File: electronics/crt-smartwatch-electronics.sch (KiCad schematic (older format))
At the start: 1 part

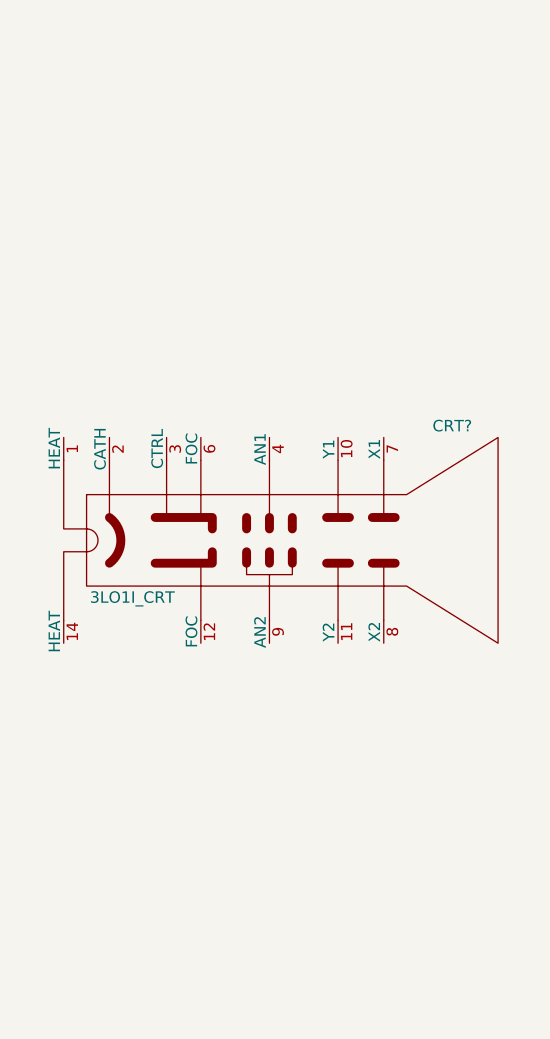
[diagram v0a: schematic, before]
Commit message: Initial connections to CRT
References:
http://www.cathodecorner.com/sc200/SC200CBoardManual.pdf
http://tubetime.us/index.php/2014/05/31/electrostatic-crt-driver-design/
https://www.youtube.com/watch?v=rDfs7nth5pQ
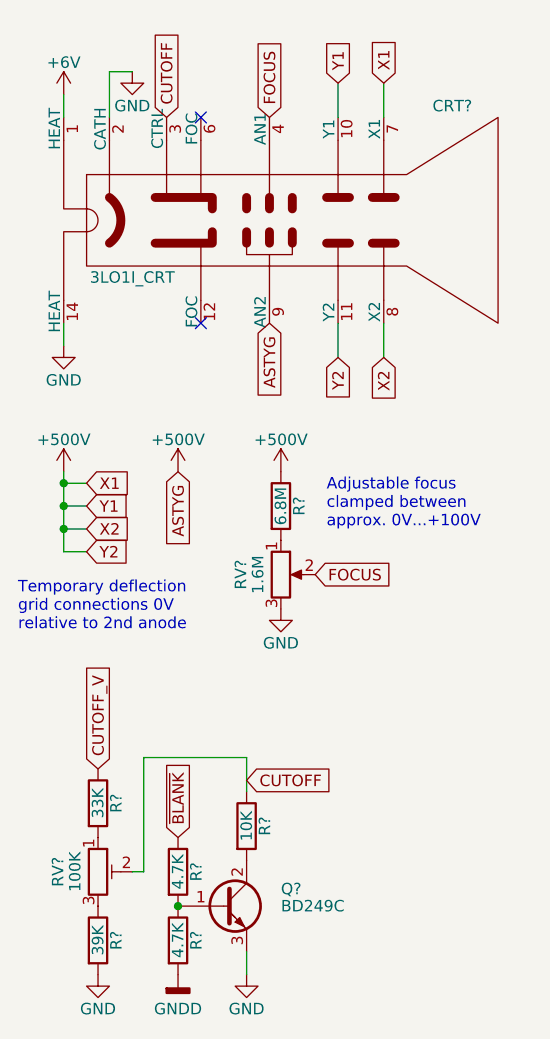
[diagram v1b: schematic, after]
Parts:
- added Q?: BD249C, symbol Transistor_BJT:BD249C
- added R?: 6.8M, symbol Device:R
- added R?: 33K, symbol Device:R
- added R?: 39K, symbol Device:R
- added R?: 10K, symbol Device:R
- added R? (x2): 4.7K, symbol Device:R
- added RV?: 1.6M, symbol Device:R_POT
- added RV?: 100K, symbol Device:R_POT_TRIM
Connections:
- net +6V: now reaches CRT?.1 (HEAT)
- net +500V: now reaches CRT?.10 (Y1)
- net +500V: now also CRT?.11 (Y2), CRT?.7 (X1), CRT?.8 (X2), CRT?.9 (AN2), R?.1
- net GND: now reaches CRT?.14 (HEAT)
- net GND: now also CRT?.2 (CATH), Q?.3 (E), R?.2, RV?.3
- net CUTOFF: now reaches CRT?.3 (CTRL)
- net CUTOFF: now also R?.1, RV?.2
- net FOCUS: now reaches CRT?.4 (AN1)
- net FOCUS: now also RV?.2
- new net: R?.2, RV?.1 (x2)
- new net: R?.1, RV?.3
- new net: Q?.1 (B), R?.1, R?.2
- new net: Q?.2 (C), R?.2
- new net CUTOFF_V: R?.1
- new net GNDD: R?.2
- new net ~BLANK: R?.1
- no-connect marks 0 -> 2
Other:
- note added: "Adjustable focus\nclamped between\napprox. 0V...+100V"
- note added: "Temporary deflection\ngrid connections 0V\nrelative to 2nd anode"
- moved on the sheet: CRT?

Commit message: Footprint for tube socket (PL-31) ordered from Amazon
https://www.amazon.com/Sockets-3LO1I-5LO2I-6LO1I-6LO2I/dp/B07Q468DZ4
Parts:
- CRT?: footprint (none) -> crt-smartwatch-footprints:PL-31_Socket
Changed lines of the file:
@@
 F 0 "CRT?" H 10800 2050 50  0000 C CNN
 F 1 "3LO1I_CRT" H 9400 1300 50  0000 C CNN
-F 2 "" H 9400 1550 50  0001 C CNN
+F 2 "crt-smartwatch-footprints:PL-31_Socket" H 9400 1550 50  0001 C CNN
 F 3 "" H 9400 1550 50  0001 C CNN
 	1    10000 1550
@@
 FOCUS
 $Comp
-L power:GND #PWR?
+L power:GND #PWR0101
 U 1 1 60A33D9B
 P 9100 2100
-F 0 "#PWR?" H 9100 1850 50  0001 C CNN
+F 0 "#PWR0101" H 9100 1850 50  0001 C CNN
 F 1 "GND" H 9100 1950 50  0000 C CNN
 F 2 "" H 9100 2100 50  0001 C CNN
@@
 	9100 2000 9100 2100
 $Comp
-L power:+6V #PWR?
+L power:+6V #PWR0102
 U 1 1 60A34C57
 P 9100 1000
-F 0 "#PWR?" H 9100 850 50  0001 C CNN
+F 0 "#PWR0102" H 9100 850 50  0001 C CNN
 F 1 "+6V" H 9100 1140 50  0000 C CNN
 F 2 "" H 9100 1000 50  0001 C CNN
@@
 	9300 900  9300 1100
 $Comp
-L power:GND #PWR?
+L power:GND #PWR0103
 U 1 1 60A36F3D
 P 9400 900
-F 0 "#PWR?" H 9400 650 50  0001 C CNN
+F 0 "#PWR0103" H 9400 650 50  0001 C CNN
 F 1 "GND" H 9400 750 50  0000 C CNN
 F 2 "" H 9400 900 50  0001 C CNN
@@
 FOCUS
 $Comp
-L crt-smartwatch-symbols:+500V #PWR?
+L crt-smartwatch-symbols:+500V #PWR0104
 U 1 1 60A40430
 P 10050 2650
-F 0 "#PWR?" H 10050 2500 50  0001 C CNN
+F 0 "#PWR0104" H 10050 2500 50  0001 C CNN
 F 1 "+500V" H 10050 2790 50  0000 C CNN
 F 2 "" H 10050 2650 50  0001 C CNN
@@
 $EndComp
 $Comp
-L power:GND #PWR?
+L power:GND #PWR0105
 U 1 1 60A40F16
 P 10050 3250
-F 0 "#PWR?" H 10050 3000 50  0001 C CNN
+F 0 "#PWR0105" H 10050 3000 50  0001 C CNN
 F 1 "GND" H 10050 3100 50  0000 C CNN
 F 2 "" H 10050 3250 50  0001 C CNN
@@
 Connection ~ 9100 2700
 $Comp
-L crt-smartwatch-symbols:+500V #PWR?
+L crt-smartwatch-symbols:+500V #PWR0106
 U 1 1 60A57ED2
 P 9100 2650
-F 0 "#PWR?" H 9100 2500 50  0001 C CNN
+F 0 "#PWR0106" H 9100 2500 50  0001 C CNN
 F 1 "+500V" H 9100 2790 50  0000 C CNN
 F 2 "" H 9100 2650 50  0001 C CNN
@@
 $EndComp
 $Comp
-L power:GND #PWR?
+L power:GND #PWR0107
 U 1 1 60A5EEAC
 P 9250 4850
-F 0 "#PWR?" H 9250 4600 50  0001 C CNN
+F 0 "#PWR0107" H 9250 4600 50  0001 C CNN
 F 1 "GND" H 9250 4700 50  0000 C CNN
 F 2 "" H 9250 4850 50  0001 C CNN
@@
 $EndComp
 $Comp
-L power:GND #PWR?
+L power:GND #PWR0108
 U 1 1 60A5F4D1
 P 9900 4850
-F 0 "#PWR?" H 9900 4600 50  0001 C CNN
+F 0 "#PWR0108" H 9900 4600 50  0001 C CNN
 F 1 "GND" H 9900 4700 50  0000 C CNN
 F 2 "" H 9900 4850 50  0001 C CNN
@@
 Connection ~ 9600 4550
 $Comp
-L power:GNDD #PWR?
+L power:GNDD #PWR0109
 U 1 1 60A6441E
 P 9600 4850
-F 0 "#PWR?" H 9600 4600 50  0001 C CNN
+F 0 "#PWR0109" H 9600 4600 50  0001 C CNN
 F 1 "GNDD" H 9600 4700 50  0000 C CNN
 F 2 "" H 9600 4850 50  0001 C CNN
@@
 ASTYG
 $Comp
-L crt-smartwatch-symbols:+500V #PWR?
+L crt-smartwatch-symbols:+500V #PWR0110
 U 1 1 60A77348
 P 9600 2650
-F 0 "#PWR?" H 9600 2500 50  0001 C CNN
+F 0 "#PWR0110" H 9600 2500 50  0001 C CNN
 F 1 "+500V" H 9600 2790 50  0000 C CNN
 F 2 "" H 9600 2650 50  0001 C CNN

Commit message: Battery monitoring circuit schematic
Reference BQ769x0 datasheet https://www.ti.com/product/BQ76920
TI also has a video helping with the schematic
https://www.youtube.com/watch?v=B5dsIc2C_xA
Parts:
- added BT?: LiPo_3s, symbol crt-smartwatch-symbols:LiPo_3s
- added C? (x2): 1u, symbol Device:C_Small
- added C? (x4): C_c, symbol Device:C_Small
- added C?: C_f, symbol Device:C_Small
- added C?: 4.7u, symbol Device:C_Small
- added C? (x3): 0.1u, symbol Device:C_Small
- added C?: 470p, symbol Device:C_Small
- added D?: 1N914, symbol Diode:1N914
- added J?: Balance, symbol Connector_Generic:Conn_01x04
- added J?: LiPo, symbol Connector_Generic:Conn_01x02
- added Q? (x2): 2N7000, Package_TO_SOT_THT:TO-92_Inline, symbol Transistor_FET:2N7000
- added Q?: VP0610L, Package_TO_SOT_THT:TO-92L_Inline, symbol Transistor_FET:VP0610L
- added R? (x4): R_c, symbol Device:R
- added R?: R_f, symbol Device:R
- added R?: R_sns, symbol Device:R
- added R? (x2): 100, symbol Device:R
- added R? (x3): 1M, symbol Device:R
- added R? (x2): 10k, symbol Device:R
- added R?: 510k, symbol Device:R
- added SW?: SW_Push, symbol Switch:SW_Push
- added U?: BQ7692006, Package_SO:TSSOP-20_4.4x6.5mm_P0.65mm, symbol Battery_Management:BQ76920PW
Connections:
- net GND: now also BT?.~ (Pack_-), C?.1, C?.1, C?.1, C?.2, C?.2, C?.2, C?.2, C?.2, C?.2, J?.2 (Pin_2), Q?.2 (G), R?.1, R?.1, R?.1, R?.1, U?.3 (VSS); no longer CRT?.14 (HEAT), CRT?.2 (CATH), Q?.3 (E), R?.2, RV?.3
- new net: C?.1, R?.2, U?.10 (BAT)
- new net: R?.1, R?.2, U?.6 (TS1)
- new net: C?.1, U?.7 (CAP1)
- new net: Q?.1 (S), R?.1, R?.1, R?.2
- new net: Q?.3 (D), Q?.3 (D)
- new net: D?.1 (K), Q?.2 (G), R?.1, R?.2
- new net: D?.2 (A), Q?.3 (D), R?.2
- new net: R?.2, SW?.1
- new net +3V3: C?.1, U?.8 (REGOUT)
- new net +BATT: BT?.~ (Pack_-), C?.2, J?.1 (Pin_1), R?.1, U?.9 (REGSRC)
- new net ALERT: C?.1, R?.2, U?.20 (ALERT)
- new net C0: C?.2, R?.2, U?.17 (VC0)
- new net C1: C?.1, C?.2, R?.2, SW?.2, U?.16 (VC1)
- new net C2: C?.1, C?.2, R?.2, U?.13 (VC4), U?.14 (VC3), U?.15 (VC2)
- new net C3: C?.1, R?.2, U?.12 (VC5)
- new net CELL_0: BT?.~ (Pack_-), J?.4 (Pin_4), R?.1
- new net CELL_1: BT?.~ (Pack_-), J?.3 (Pin_3), R?.1
- new net CELL_2: BT?.~ (Pack_-), J?.2 (Pin_2), R?.1
- new net CELL_3: BT?.~ (Pack_-), J?.1 (Pin_1), R?.1
- new net CHG: Q?.1 (S), U?.2 (CHG)
- new net DSG: Q?.2 (G), R?.2, U?.1 (DSG)
- new net GND1: CRT?.14 (HEAT), CRT?.2 (CATH), Q?.1 (S), Q?.3 (E), R?.1, R?.2, RV?.3
- new net SCL: U?.5 (SCL)
- new net SDA: U?.4 (SDA)
- new net SRN: C?.1, C?.2, R?.2, U?.19 (SRN)
- new net SRP: C?.1, C?.2, R?.2, U?.18 (SRP)
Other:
- note added: "Battery and connectors"
- note added: "Battery current measuring\nresistor and RC filters"
- note added: "Battery monitor IC"
- note added: "Cell voltage sensing RC filters"
- note added: "Low-side MOSFET power\ncuttoff circuit"

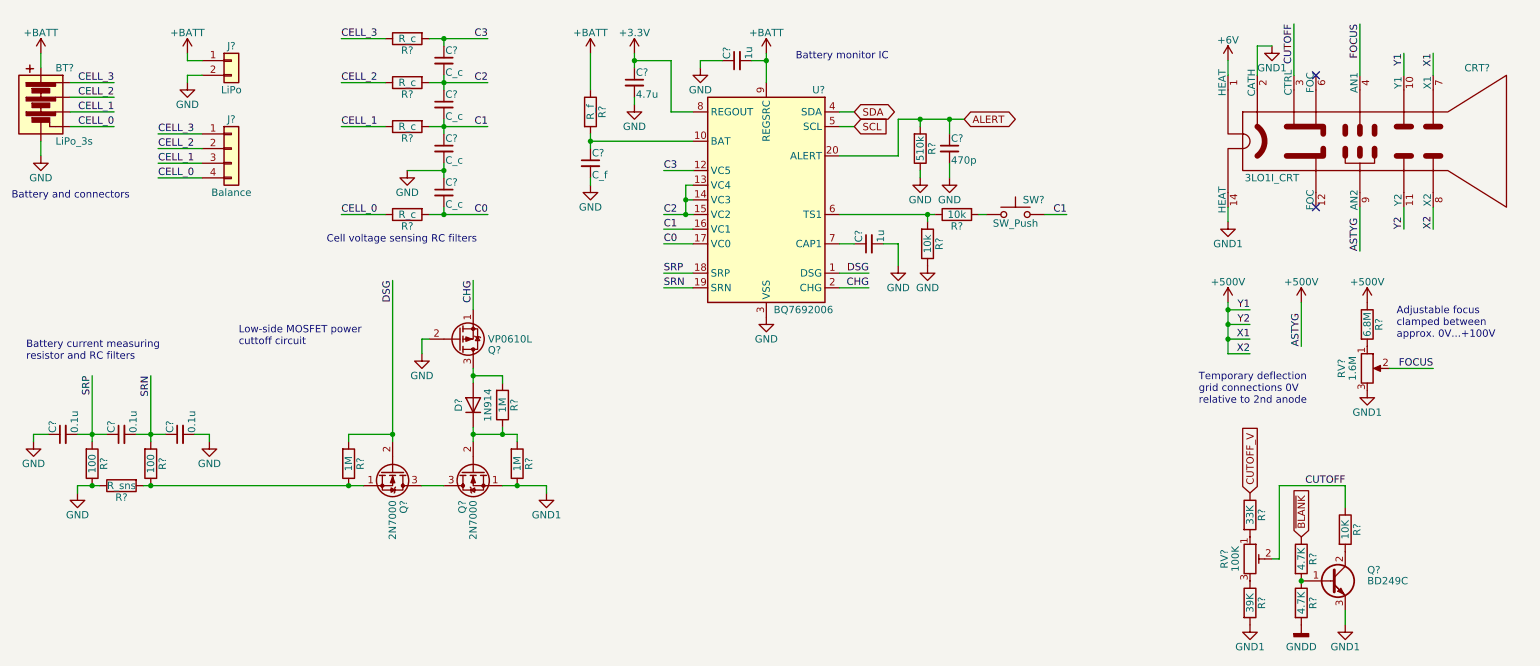
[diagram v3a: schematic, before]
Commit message: Compartmentalized schematic circuits into separate sheets
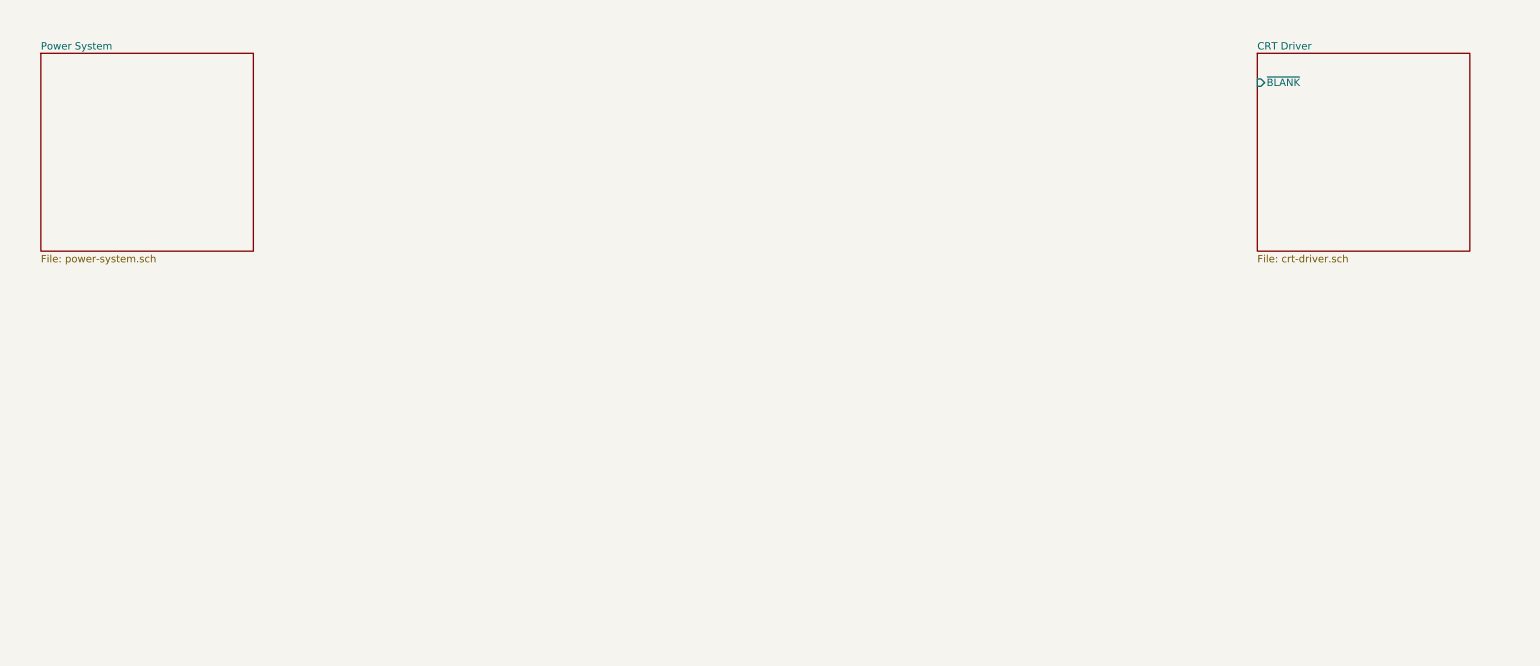
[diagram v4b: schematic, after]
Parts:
- removed BT?: LiPo_3s, symbol crt-smartwatch-symbols:LiPo_3s
- removed C? (x2): 1u, symbol Device:C_Small
- removed C? (x4): C_c, symbol Device:C_Small
- removed C?: C_f, symbol Device:C_Small
- removed C?: 4.7u, symbol Device:C_Small
- removed C? (x3): 0.1u, symbol Device:C_Small
- removed C?: 470p, symbol Device:C_Small
- removed CRT?: 3LO1I_CRT, crt-smartwatch-footprints:PL-31_Socket, symbol crt-smartwatch-symbols:3LO1I_CRT
- removed D?: 1N914, symbol Diode:1N914
- removed J?: Balance, symbol Connector_Generic:Conn_01x04
- removed J?: LiPo, symbol Connector_Generic:Conn_01x02
- removed Q?: BD249C, symbol Transistor_BJT:BD249C
- removed Q? (x2): 2N7000, Package_TO_SOT_THT:TO-92_Inline, symbol Transistor_FET:2N7000
- removed Q?: VP0610L, Package_TO_SOT_THT:TO-92L_Inline, symbol Transistor_FET:VP0610L
- removed R?: 6.8M, symbol Device:R
- removed R?: 33K, symbol Device:R
- removed R?: 39K, symbol Device:R
- removed R?: 10K, symbol Device:R
- removed R? (x2): 4.7K, symbol Device:R
- removed R? (x4): R_c, symbol Device:R
- removed R?: R_f, symbol Device:R
- removed R?: R_sns, symbol Device:R
- removed R? (x2): 100, symbol Device:R
- removed R? (x3): 1M, symbol Device:R
- removed R? (x2): 10k, symbol Device:R
- removed R?: 510k, symbol Device:R
- removed RV?: 1.6M, symbol Device:R_POT
- removed RV?: 100K, symbol Device:R_POT_TRIM
- removed SW?: SW_Push, symbol Switch:SW_Push
- removed U?: BQ7692006, Package_SO:TSSOP-20_4.4x6.5mm_P0.65mm, symbol Battery_Management:BQ76920PW
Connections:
- no-connect marks 2 -> 0
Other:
- note removed: "Adjustable focus\nclamped between\napprox. 0V...+100V"
- note removed: "Battery and connectors"
- note removed: "Battery current measuring\nresistor and RC filters"
- note removed: "Battery monitor IC"
- note removed: "Cell voltage sensing RC filters"
- note removed: "Low-side MOSFET power\ncuttoff circuit"
- note removed: "Temporary deflection\ngrid connections 0V\nrelative to 2nd anode"

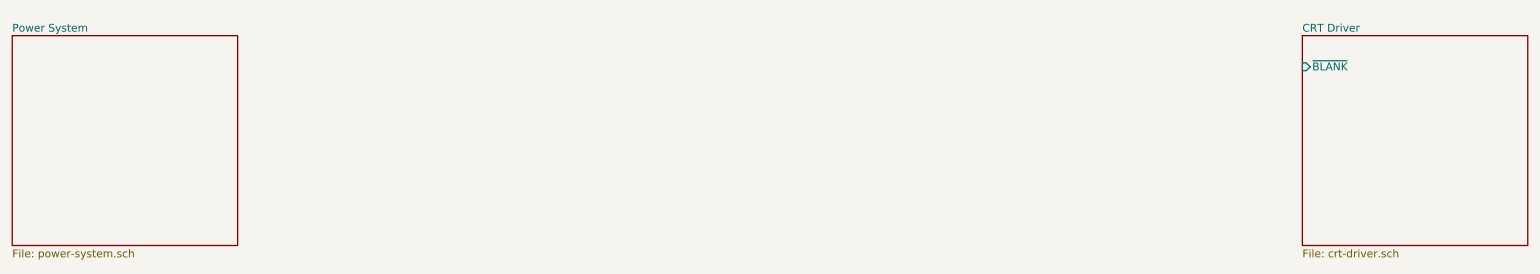
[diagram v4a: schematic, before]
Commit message: Design notes for 3.3V LDR and schematic updates
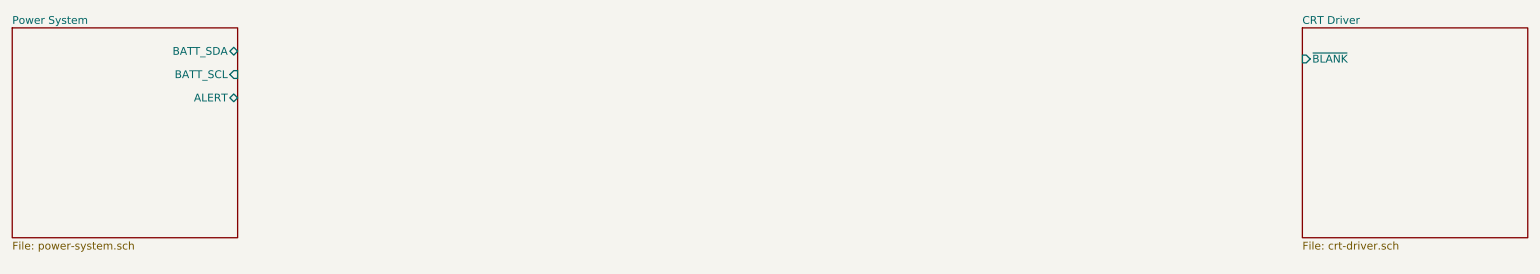
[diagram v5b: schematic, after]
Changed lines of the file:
@@
 $EndDescr
 $Sheet
-S 9300 950  1450 1350
+S 9300 900  1450 1350
 U 6113F6B3
 F0 "CRT Driver" 50
 F1 "crt-driver.sch" 50
-F2 "~BLANK" I L 9300 1150 50
+F2 "~BLANK" I L 9300 1100 50
 $EndSheet
 $Sheet
-S 1000 950  1450 1350
+S 1000 900  1450 1350
 U 611ADD88
 F0 "Power System" 50
 F1 "power-system.sch" 50
+F2 "BATT_SDA" B R 2450 1050 50
+F3 "BATT_SCL" I R 2450 1200 50
+F4 "ALERT" B R 2450 1350 50
 $EndSheet
 $EndSCHEMATC

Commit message: PIC32 Power Sequencing Microcontroller
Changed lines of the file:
@@
 $Descr A4 11693 8268
 encoding utf-8
-Sheet 1 3
+Sheet 1 4
 Title "CRT Smartwatch"
 Date ""
@@
 F4 "ALERT" B R 2450 1350 50
 $EndSheet
+$Sheet
+S 3000 900  1400 1350
+U 60C1AF78
+F0 "PIC32 Microcontroller" 50
+F1 "pic32-microcontroller.sch" 50
+F2 "PIC_SDA" B L 3000 1050 50
+F3 "PIC_SCL" O L 3000 1200 50
+F4 "ALERT" B L 3000 1350 50
+F5 "A" I R 4400 1050 50
+F6 "~B" I R 4400 1200 50
+F7 "~Z" O R 4400 1450 50
+F8 "Y" O R 4400 1600 50
+$EndSheet
+Wire Wire Line
+	2450 1050 3000 1050
+Wire Wire Line
+	2450 1200 3000 1200
+Wire Wire Line
+	2450 1350 3000 1350
 $EndSCHEMATC
